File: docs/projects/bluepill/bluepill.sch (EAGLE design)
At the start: 10 parts

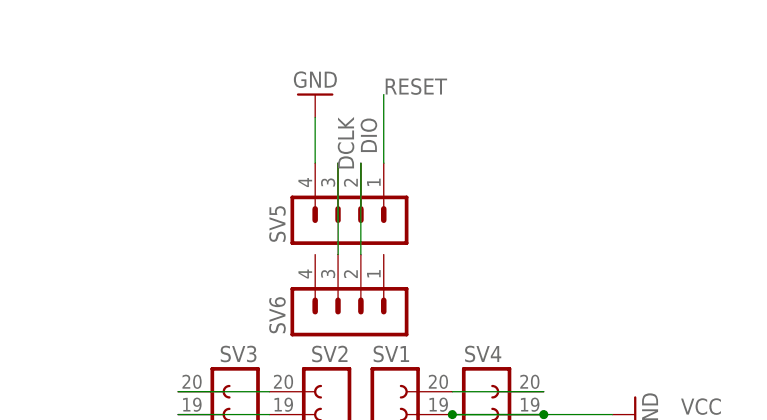
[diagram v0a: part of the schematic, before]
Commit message: bluepill: fix order
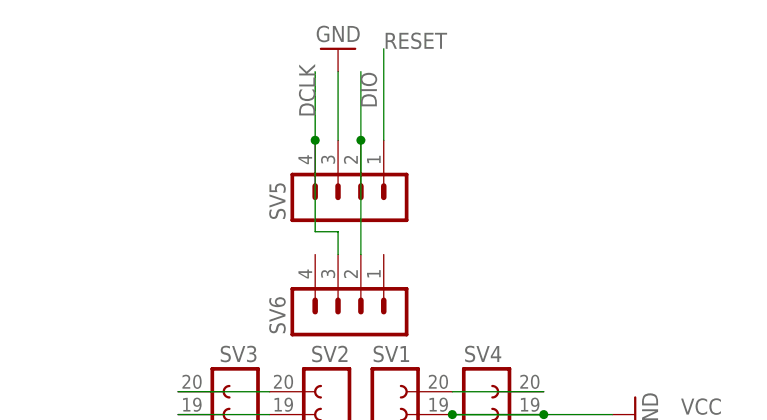
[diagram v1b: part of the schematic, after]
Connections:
- net DCLK: now also SV5.4; no longer SV5.3
- net GND: now also SV5.3; no longer SV5.4
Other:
- moved on the sheet: SV5
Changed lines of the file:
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@@
 <instance part="SV3" gate="G$1" x="114.3" y="170.18" rot="MR0"/>
 <instance part="SV4" gate="G$1" x="139.7" y="170.18"/>
-<instance part="SV5" gate="1" x="124.46" y="210.82" rot="R90"/>
+<instance part="SV5" gate="1" x="124.46" y="213.36" rot="R90"/>
 <instance part="S1" gate="1" x="190.5" y="154.94"/>
 <instance part="GND7" gate="1" x="190.5" y="144.78"/>
 <instance part="SV6" gate="1" x="124.46" y="200.66" rot="R90"/>
 <instance part="GND3" gate="1" x="111.76" y="60.96" rot="R270"/>
-<instance part="GND1" gate="1" x="121.92" y="226.06" rot="R180"/>
+<instance part="GND1" gate="1" x="124.46" y="231.14" rot="R180"/>
 </instances>
 <busses>
@@
 </segment>
 <segment>
-<pinref part="SV5" gate="1" pin="4"/>
 <pinref part="GND1" gate="1" pin="GND"/>
-<wire x1="121.92" y1="223.52" x2="121.92" y2="218.44" width="0.1524" layer="91"/>
+<pinref part="SV5" gate="1" pin="3"/>
+<wire x1="124.46" y1="228.6" x2="124.46" y2="220.98" width="0.1524" layer="91"/>
 </segment>
 </net>
@@
 <segment>
 <pinref part="SV5" gate="1" pin="1"/>
-<wire x1="129.54" y1="218.44" x2="129.54" y2="226.06" width="0.1524" layer="91"/>
-<label x="129.54" y="226.06" size="1.778" layer="95"/>
+<wire x1="129.54" y1="220.98" x2="129.54" y2="231.14" width="0.1524" layer="91"/>
+<label x="129.54" y="231.14" size="1.778" layer="95"/>
 </segment>
 </net>
@@
 <segment>
 <pinref part="SV5" gate="1" pin="2"/>
-<wire x1="127" y1="218.44" x2="127" y2="208.28" width="0.1524" layer="91"/>
-<label x="127" y="223.52" size="1.778" layer="95" rot="R270"/>
+<wire x1="127" y1="220.98" x2="127" y2="208.28" width="0.1524" layer="91"/>
+<label x="127" y="228.6" size="1.778" layer="95" rot="R270"/>
 <pinref part="SV6" gate="1" pin="2"/>
+<wire x1="127" y1="220.98" x2="127" y2="228.6" width="0.1524" layer="91"/>
+<junction x="127" y="220.98"/>
 </segment>
 </net>
 <net name="DCLK" class="0">
 <segment>
-<pinref part="SV5" gate="1" pin="3"/>
-<wire x1="124.46" y1="218.44" x2="124.46" y2="208.28" width="0.1524" layer="91"/>
-<label x="124.46" y="223.52" size="1.778" layer="95" rot="R270"/>
 <pinref part="SV6" gate="1" pin="3"/>
-</segment>
-</net>
+<wire x1="124.46" y1="208.28" x2="124.46" y2="210.82" width="0.1524" layer="91"/>
+<wire x1="124.46" y1="210.82" x2="121.92" y2="210.82" width="0.1524" layer="91"/>
+<wire x1="121.92" y1="210.82" x2="121.92" y2="220.98" width="0.1524" layer="91"/>
+<pinref part="SV5" gate="1" pin="4"/>
+<wire x1="121.92" y1="220.98" x2="121.92" y2="228.6" width="0.1524" layer="91"/>
+<label x="121.92" y="223.52" size="1.778" layer="95" rot="R90"/>
+<junction x="121.92" y="220.98"/>
+</segment>
+</net>
